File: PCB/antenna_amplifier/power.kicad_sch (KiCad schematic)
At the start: 20 parts, among them J101 DC IN, U101 ADM7150ARDZ-5.0, U102 ADM7150ARDZ-3.3

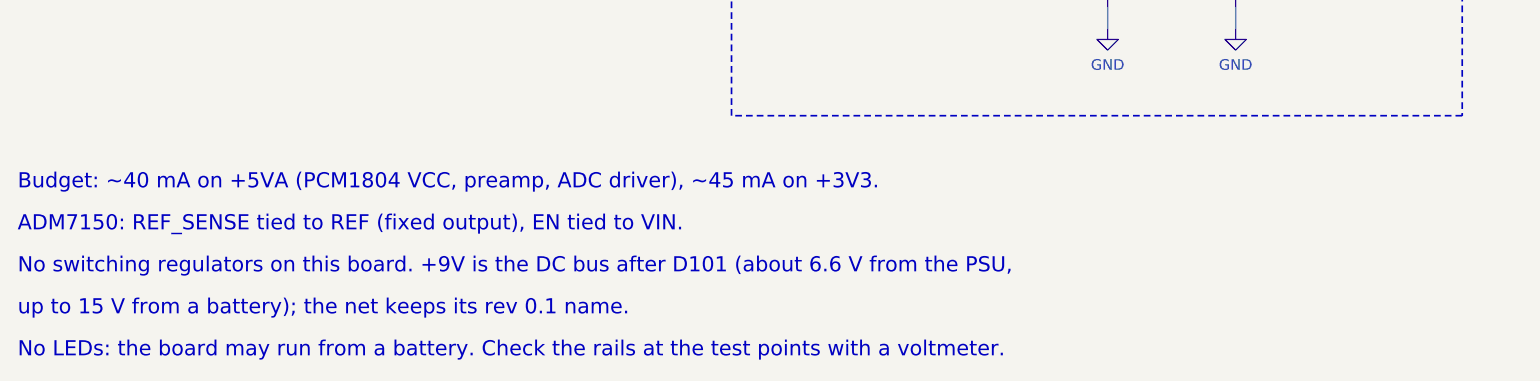
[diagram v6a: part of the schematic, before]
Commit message: PSU charger at 10.4 V so the 2.7 V cells stay in rating; charger model corrected
The LM317 CV divider (240 R / 1.87 k) set 11.08 V, not the 10.9 V it was
labelled with: 2.72 V per EDLC cell whenever the receiver draws nothing,
2.83 V at the LM317's limits. R4 is now 1.74 k (10.4 V, 2.55 V per cell,
2.70 V worst case). Board copper and placement are unchanged; only R4's
value, the BOM and the order lists change.

The PSU model's charger now drops 6.2 ohm x I in the CC stage below 0.2 A
instead of a fixed 1.25 V. Re-run: 1.81 V of LT3045 headroom nominal,
1.05 V with every corner stacked. A 30 s swap is added as an option case
(0.36 V stacked), which replaces STATUS's unbacked claim that it drops out.
Also: the amplifier's +9V bus is about 6.0 V from the PSU (not 6.6 V),
and the PSU README's circuit line, CMC loop and margin figures are fixed.

Co-Authored-By: Claude Opus 5.5 <noreply@anthropic.com>
Claude-Session: https://claude.ai/code/session_01RsM1DhHhY1tSr2aHjVygSC
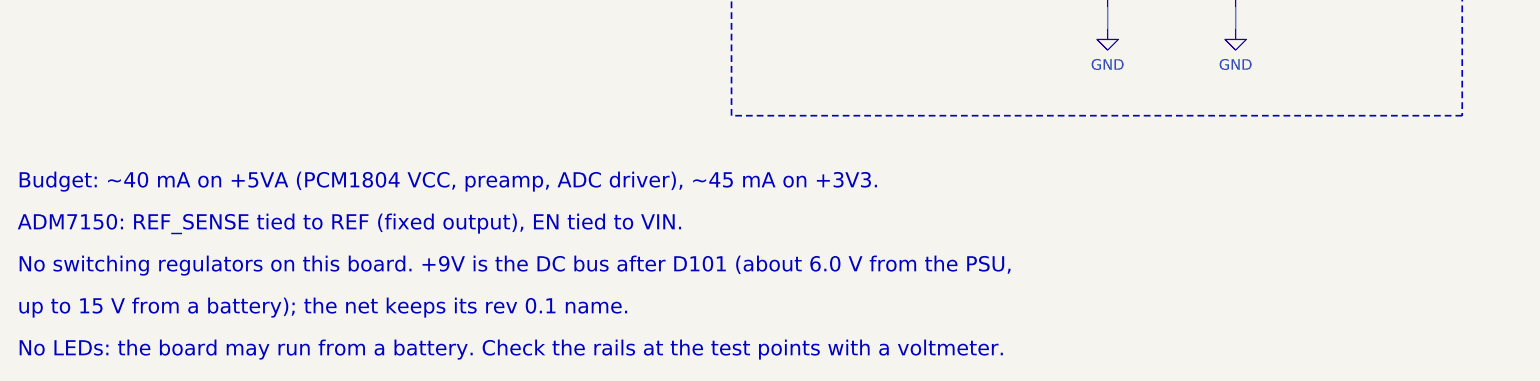
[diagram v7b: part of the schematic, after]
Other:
- note added: "No switching regulators on this board. +9V is the DC bus after D101 (about 6.0 V from the PSU,"
- note removed: "No switching regulators on this board. +9V is the DC bus after D101 (about 6.6 V from the PSU,"
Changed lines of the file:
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@@
 		)
 	)
-	(text "No switching regulators on this board. +9V is the DC bus after D101 (about 6.6 V from the PSU,"
+	(text "No switching regulators on this board. +9V is the DC bus after D101 (about 6.0 V from the PSU,"
 		(exclude_from_sim no)
 		(at 15 150 0)
